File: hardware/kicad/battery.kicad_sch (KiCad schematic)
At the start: 3 parts, among them Q1 AO3407

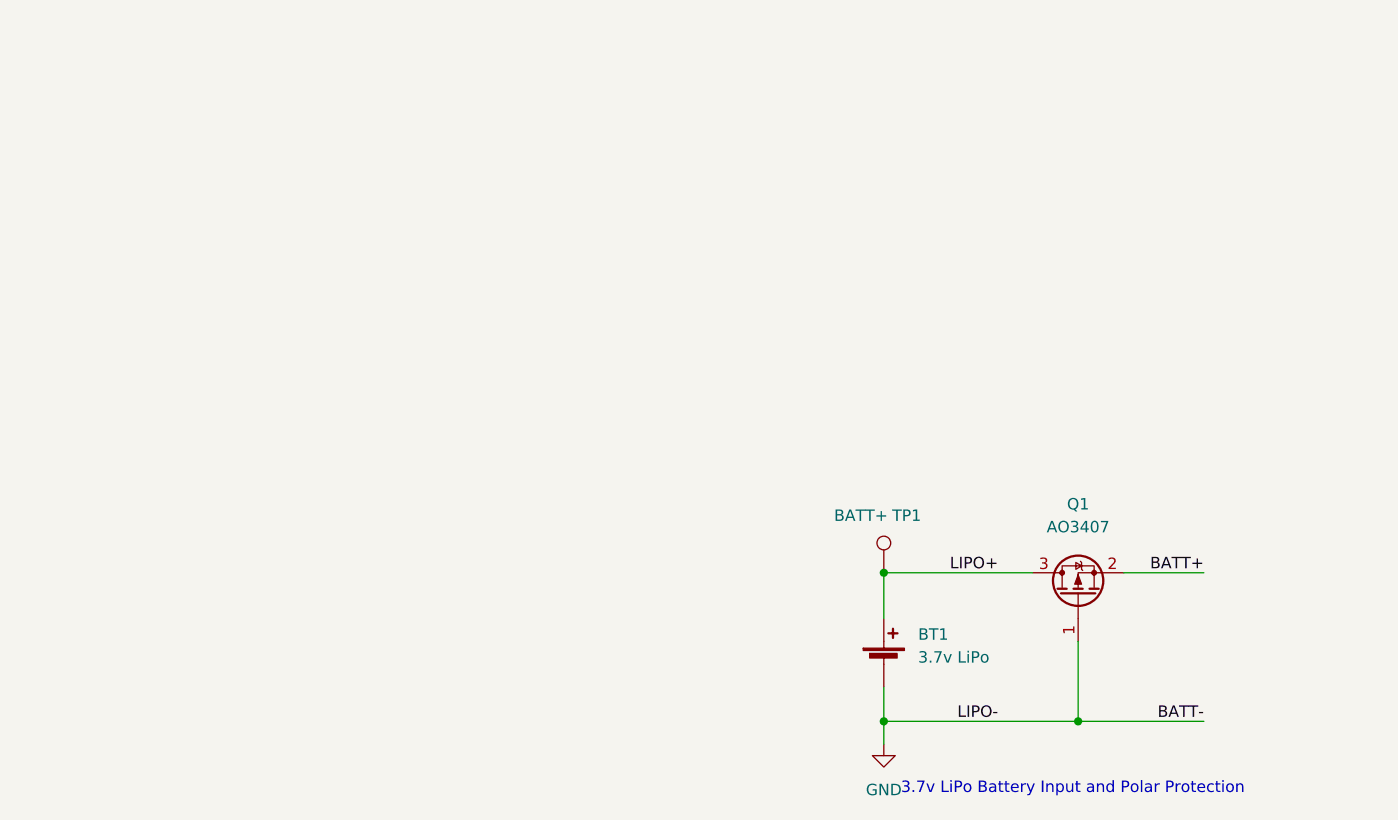
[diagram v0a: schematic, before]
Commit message: fix label
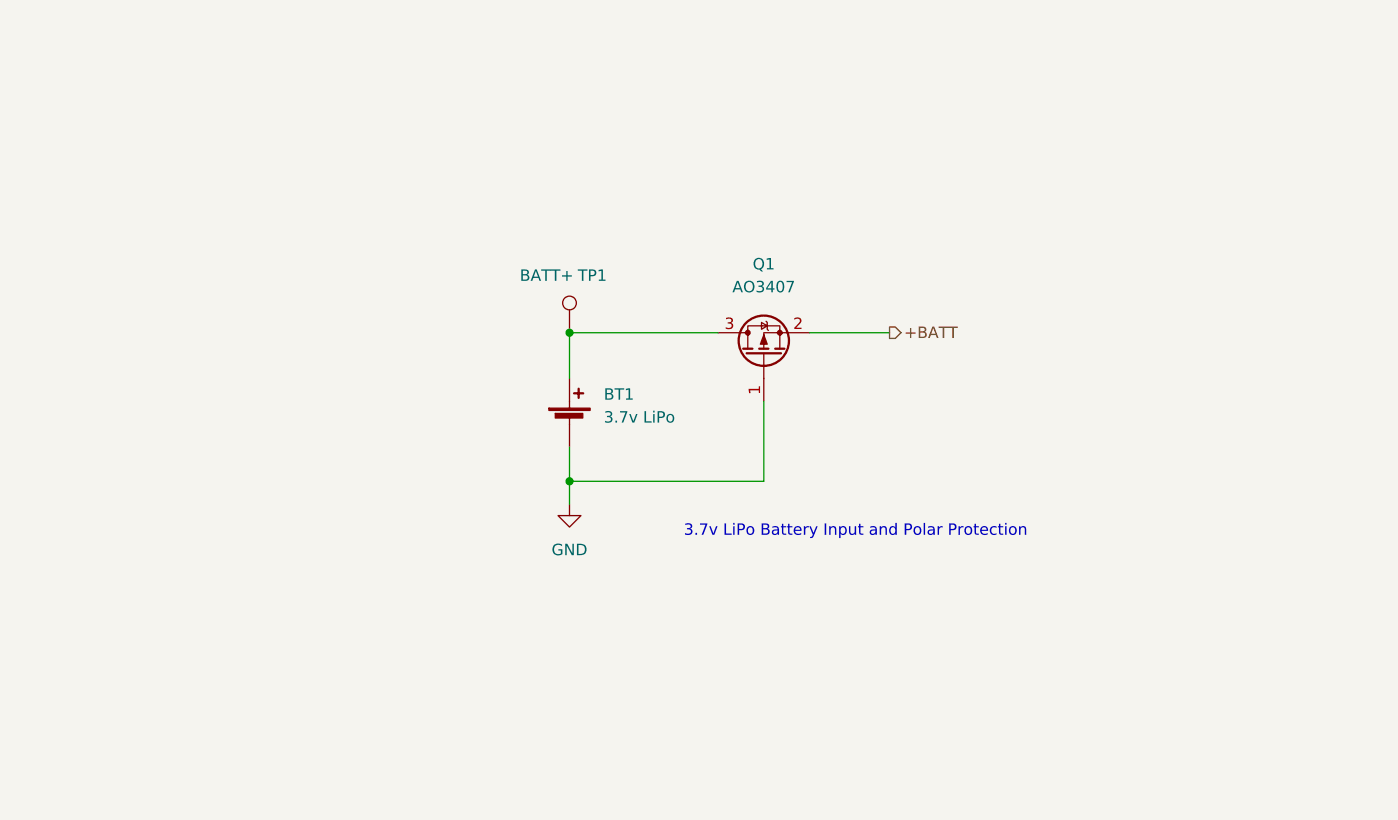
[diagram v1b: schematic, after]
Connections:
- net BATT+ renamed +BATT
- net LIPO+: no longer names the net of BT1.1 (+), Q1.3 (D), TP1.1
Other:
- moved on the sheet: BT1, Q1, TP1
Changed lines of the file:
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@@
 (kicad_sch (version 20230121) (generator eeschema)
-  (paper "A4")
-  (junction (at 114.3 79.375) (diameter 0) (color 0 0 0 0)
+  (paper "A5")
+  (junction (at 79.375 52.705) (diameter 0) (color 0 0 0 0)
   )
-  (junction (at 114.3 95.885) (diameter 0) (color 0 0 0 0)
+  (junction (at 79.375 69.215) (diameter 0) (color 0 0 0 0)
   )
-  (junction (at 135.89 95.885) (diameter 0) (color 0 0 0 0)
-  )
-  (wire (pts (xy 135.89 86.995) (xy 135.89 95.885))
+  (wire (pts (xy 100.965 60.325) (xy 100.965 69.215))
     (stroke (width 0) (type default))
   )
-  (wire (pts (xy 135.89 95.885) (xy 149.86 95.885))
+  (wire (pts (xy 79.375 52.705) (xy 79.375 57.785))
     (stroke (width 0) (type default))
   )
-  (wire (pts (xy 114.3 79.375) (xy 114.3 84.455))
+  (wire (pts (xy 106.045 52.705) (xy 114.935 52.705))
     (stroke (width 0) (type default))
   )
-  (wire (pts (xy 140.97 79.375) (xy 149.86 79.375))
+  (wire (pts (xy 79.375 69.215) (xy 79.375 71.755))
     (stroke (width 0) (type default))
   )
-  (wire (pts (xy 114.3 95.885) (xy 114.3 98.425))
+  (wire (pts (xy 79.375 65.405) (xy 79.375 69.215))
     (stroke (width 0) (type default))
   )
-  (wire (pts (xy 114.3 92.075) (xy 114.3 95.885))
+  (wire (pts (xy 79.375 69.215) (xy 100.965 69.215))
     (stroke (width 0) (type default))
   )
-  (wire (pts (xy 114.3 95.885) (xy 135.89 95.885))
+  (wire (pts (xy 79.375 52.705) (xy 95.885 52.705))
     (stroke (width 0) (type default))
   )
-  (wire (pts (xy 114.3 79.375) (xy 130.81 79.375))
-    (stroke (width 0) (type default))
-  )
-  (text "3.7v LiPo Battery Input and Polar Protection" (at 116.205 104.14 0)
+  (text "3.7v LiPo Battery Input and Polar Protection" (at 92.075 75.565 0)
     (effects (font (size 1.27 1.27)) (justify left bottom))
   )
-  (label "LIPO-" (at 127 95.885 180) (fields_autoplaced)
-    (effects (font (size 1.27 1.27)) (justify right bottom))
+  (hierarchical_label "+BATT" (shape output) (at 114.935 52.705 0) (fields_autoplaced)
+    (effects (font (size 1.27 1.27)) (justify left))
   )
-  (label "LIPO+" (at 127 79.375 180) (fields_autoplaced)
-    (effects (font (size 1.27 1.27)) (justify right bottom))
-  )
-  (label "BATT+" (at 149.86 79.375 180) (fields_autoplaced)
-    (effects (font (size 1.27 1.27)) (justify right bottom))
-  )
-  (label "BATT-" (at 149.86 95.885 180) (fields_autoplaced)
-    (effects (font (size 1.27 1.27)) (justify right bottom))
-  )
-  (symbol (lib_id "Device:Q_PMOS_GSD") (at 135.89 81.915 90) (unit 1)
+  (symbol (lib_id "Device:Q_PMOS_GSD") (at 100.965 55.245 90) (unit 1)
     (in_bom yes) (on_board yes) (dnp no) (fields_autoplaced)
-    (property "Reference" "Q1" (at 135.89 71.755 90)
+    (property "Reference" "Q1" (at 100.965 45.085 90)
       (effects (font (size 1.27 1.27)))
     )
-    (property "Value" "AO3407" (at 135.89 74.295 90)
+    (property "Value" "AO3407" (at 100.965 47.625 90)
       (effects (font (size 1.27 1.27)))
     )
-    (property "Footprint" "Package_TO_SOT_SMD:SOT-23" (at 133.35 76.835 0)
+    (property "Footprint" "Package_TO_SOT_SMD:SOT-23" (at 98.425 50.165 0)
       (effects (font (size 1.27 1.27)) hide)
     )
-    (property "Datasheet" "~" (at 135.89 81.915 0)
+    (property "Datasheet" "~" (at 100.965 55.245 0)
       (effects (font (size 1.27 1.27)) hide)
     )
@@
     )
   )
-  (symbol (lib_id "Connector:TestPoint") (at 114.3 79.375 0) (unit 1)
+  (symbol (lib_id "Connector:TestPoint") (at 79.375 52.705 0) (unit 1)
     (in_bom yes) (on_board yes) (dnp no)
-    (property "Reference" "TP1" (at 116.84 73.025 0)
+    (property "Reference" "TP1" (at 81.915 46.355 0)
       (effects (font (size 1.27 1.27)))
     )
-    (property "Value" "BATT+" (at 111.76 73.025 0)
+    (property "Value" "BATT+" (at 76.835 46.355 0)
       (effects (font (size 1.27 1.27)))
     )
-    (property "Footprint" "TestPoint:TestPoint_Pad_D1.5mm" (at 119.38 79.375 0)
+    (property "Footprint" "TestPoint:TestPoint_Pad_D1.5mm" (at 84.455 52.705 0)
       (effects (font (size 1.27 1.27)) hide)
     )
-    (property "Datasheet" "~" (at 119.38 79.375 0)
+    (property "Datasheet" "~" (at 84.455 52.705 0)
       (effects (font (size 1.27 1.27)) hide)
     )
@@
     )
   )
-  (symbol (lib_id "Device:Battery_Cell") (at 114.3 89.535 0) (unit 1)
+  (symbol (lib_id "Device:Battery_Cell") (at 79.375 62.865 0) (unit 1)
     (in_bom yes) (on_board yes) (dnp no) (fields_autoplaced)
-    (property "Reference" "BT1" (at 118.11 86.2329 0)
+    (property "Reference" "BT1" (at 83.185 59.5629 0)
       (effects (font (size 1.27 1.27)) (justify left))
     )
-    (property "Value" "3.7v LiPo" (at 118.11 88.7729 0)
+    (property "Value" "3.7v LiPo" (at 83.185 62.1029 0)
       (effects (font (size 1.27 1.27)) (justify left))
     )
-    (property "Footprint" "Connector_JST:JST_PH_S2B-PH-K_1x02_P2.00mm_Horizontal" (at 114.3 88.011 90)
+    (property "Footprint" "Connector_JST:JST_PH_S2B-PH-K_1x02_P2.00mm_Horizontal" (at 79.375 61.341 90)
       (effects (font (size 1.27 1.27)) hide)
     )
-    (property "Datasheet" "~" (at 114.3 88.011 90)
+    (property "Datasheet" "~" (at 79.375 61.341 90)
       (effects (font (size 1.27 1.27)) hide)
     )
@@
     )
   )
-  (symbol (lib_id "power:GND") (at 114.3 98.425 0) (unit 1)
+  (symbol (lib_id "power:GND") (at 79.375 71.755 0) (unit 1)
     (in_bom yes) (on_board yes) (dnp no)
-    (property "Reference" "#PWR06" (at 114.3 104.775 0)
+    (property "Reference" "#PWR06" (at 79.375 78.105 0)
       (effects (font (size 1.27 1.27)) hide)
     )
-    (property "Value" "GND" (at 114.3 103.505 0)
+    (property "Value" "GND" (at 79.375 76.835 0)
       (effects (font (size 1.27 1.27)))
     )
-    (property "Footprint" "" (at 114.3 98.425 0)
+    (property "Footprint" "" (at 79.375 71.755 0)
       (effects (font (size 1.27 1.27)) hide)
     )
-    (property "Datasheet" "" (at 114.3 98.425 0)
+    (property "Datasheet" "" (at 79.375 71.755 0)
       (effects (font (size 1.27 1.27)) hide)
     )

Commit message: schematic restructure update
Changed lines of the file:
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@@
+    (stroke (width 0) (type default))
+  )
+  (wire (pts (xy 115.57 48.895) (xy 115.57 52.705))
     (stroke (width 0) (type default))
   )
@@
     (stroke (width 0) (type default))
   )
-  (wire (pts (xy 106.045 52.705) (xy 114.935 52.705))
+  (wire (pts (xy 106.045 52.705) (xy 115.57 52.705))
+    (stroke (width 0) (type default))
+  )
+  (wire (pts (xy 21.59 23.495) (xy 21.59 26.035))
     (stroke (width 0) (type default))
   )
@@
   )
   (wire (pts (xy 79.375 69.215) (xy 100.965 69.215))
+    (stroke (width 0) (type default))
+  )
+  (wire (pts (xy 21.59 26.035) (xy 27.305 26.035))
     (stroke (width 0) (type default))
   )
@@
     (effects (font (size 1.27 1.27)) (justify left bottom))
   )
-  (hierarchical_label "+BATT" (shape output) (at 114.935 52.705 0) (fields_autoplaced)
+  (hierarchical_label "+BATT" (shape bidirectional) (at 27.305 26.035 0) (fields_autoplaced)
     (effects (font (size 1.27 1.27)) (justify left))
   )
@@
         )
         (path "/59b4123e-c7be-466b-a5db-658b8f0c1171/76cc1a03-b597-4ef0-85b8-85a2d617e76b"
+          (reference "Q6") (unit 1)
+        )
+      )
+      (project "bwlr1e"
+        (path "/630c8da6-5464-4eef-824d-89618087f4b4"
           (reference "Q1") (unit 1)
         )
       )
-      (project "bwlr1e"
-        (path "/630c8da6-5464-4eef-824d-89618087f4b4"
-          (reference "Q1") (unit 1)
-        )
-      )
     )
   )
@@
         )
         (path "/59b4123e-c7be-466b-a5db-658b8f0c1171/76cc1a03-b597-4ef0-85b8-85a2d617e76b"
-          (reference "TP1") (unit 1)
+          (reference "TP6") (unit 1)
         )
       )
@@
     )
   )
+  (symbol (lib_id "power:+BATT") (at 115.57 48.895 0) (unit 1)
+    (in_bom yes) (on_board yes) (dnp no)
+    (property "Reference" "#PWR070" (at 115.57 52.705 0)
+      (effects (font (size 1.27 1.27)) hide)
+    )
+    (property "Value" "+BATT" (at 115.57 44.45 0)
+      (effects (font (size 1.27 1.27)))
+    )
+    (property "Footprint" "" (at 115.57 48.895 0)
+      (effects (font (size 1.27 1.27)) hide)
+    )
+    (property "Datasheet" "" (at 115.57 48.895 0)
+      (effects (font (size 1.27 1.27)) hide)
+    )
+    (pin "1")
+    (instances
+      (project "plantpal"
+        (path "/59b4123e-c7be-466b-a5db-658b8f0c1171"
+          (reference "#PWR070") (unit 1)
+        )
+        (path "/59b4123e-c7be-466b-a5db-658b8f0c1171/7fda2409-1758-4461-822b-801ba75fe202"
+          (reference "#PWR050") (unit 1)
+        )
+        (path "/59b4123e-c7be-466b-a5db-658b8f0c1171/76cc1a03-b597-4ef0-85b8-85a2d617e76b"
+          (reference "#PWR078") (unit 1)
+        )
+      )
+      (project "bwlr1e-prog"
+        (path "/630c8da6-5464-4eef-824d-89618087f4b4"
+          (reference "#PWR018") (unit 1)
+        )
+      )
+      (project "feather_rak3172"
+        (path "/a1545928-1195-40b9-b3c4-78f837012afb"
+          (reference "#PWR0131") (unit 1)
+        )
+      )
+    )
+  )
   (symbol (lib_id "power:GND") (at 79.375 71.755 0) (unit 1)
     (in_bom yes) (on_board yes) (dnp no)
@@
         )
         (path "/59b4123e-c7be-466b-a5db-658b8f0c1171/76cc1a03-b597-4ef0-85b8-85a2d617e76b"
-          (reference "#PWR06") (unit 1)
+          (reference "#PWR077") (unit 1)
         )
       )
@@
         )
       )
+    )
+  )
+  (symbol (lib_id "power:+BATT") (at 21.59 23.495 0) (unit 1)
+    (in_bom yes) (on_board yes) (dnp no)
+    (property "Reference" "#PWR070" (at 21.59 27.305 0)
+      (effects (font (size 1.27 1.27)) hide)
+    )
+    (property "Value" "+BATT" (at 21.59 19.05 0)
+      (effects (font (size 1.27 1.27)))
+    )
+    (property "Footprint" "" (at 21.59 23.495 0)
+      (effects (font (size 1.27 1.27)) hide)
+    )
+    (property "Datasheet" "" (at 21.59 23.495 0)
+      (effects (font (size 1.27 1.27)) hide)
+    )
+    (pin "1")
+    (instances
+      (project "plantpal"
+        (path "/59b4123e-c7be-466b-a5db-658b8f0c1171"
+          (reference "#PWR070") (unit 1)
+        )
+        (path "/59b4123e-c7be-466b-a5db-658b8f0c1171/7fda2409-1758-4461-822b-801ba75fe202"
+          (reference "#PWR050") (unit 1)
+        )
+        (path "/59b4123e-c7be-466b-a5db-658b8f0c1171/76cc1a03-b597-4ef0-85b8-85a2d617e76b"
+          (reference "#PWR079") (unit 1)
+        )
+      )
+      (project "bwlr1e-prog"
+        (path "/630c8da6-5464-4eef-824d-89618087f4b4"
+          (reference "#PWR018") (unit 1)
+        )
+      )
+      (project "feather_rak3172"
+        (path "/a1545928-1195-40b9-b3c4-78f837012afb"
+          (reference "#PWR0131") (unit 1)
+        )
+      )

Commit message: beautify schematic
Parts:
- TP1: value BATT+ -> +LIPO
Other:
- note added: "Battery Polar Protection"
- note added: "Sheets Connection"
- note removed: "3.7v LiPo Battery Input and Polar Protection"
- moved on the sheet: BT1, Q1, TP1

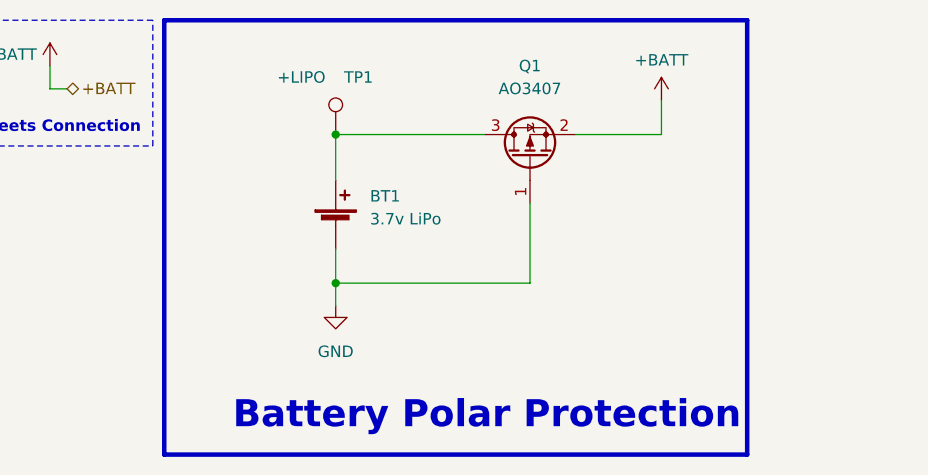
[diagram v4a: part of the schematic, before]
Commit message: battery schematic done
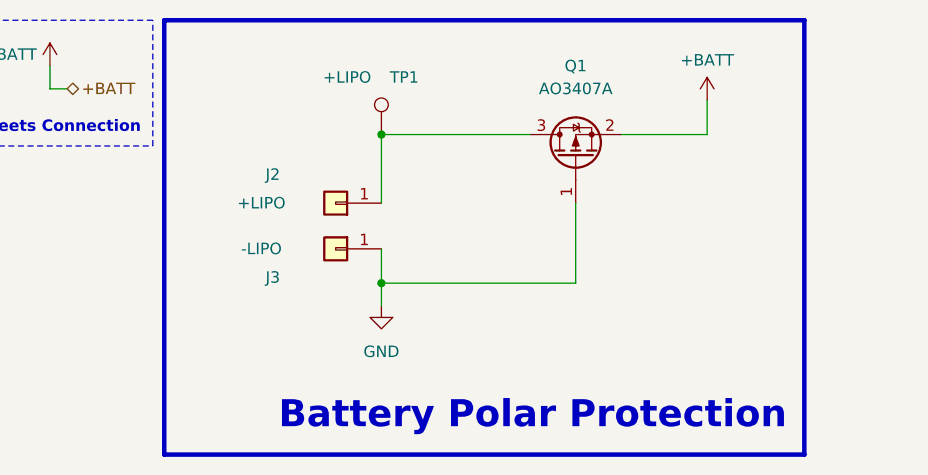
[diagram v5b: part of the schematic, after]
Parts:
- removed BT1: 3.7v LiPo, Connector_JST:JST_PH_S2B-PH-K_1x02_P2.00mm_Horizontal, symbol Device:Battery_Cell
- added J2: +LIPO, TestPoint:TestPoint_Pad_2.0x2.0mm, symbol Connector_Generic:Conn_01x01
- added J3: -LIPO, TestPoint:TestPoint_Pad_2.0x2.0mm, symbol Connector_Generic:Conn_01x01
- Q1: value AO3407 -> AO3407A; Distributor (none) -> LCSC; Distributor Link (none) -> https://www.lcsc.com/product-detail/MOSFETs_Alpha-Omega-Sem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; Distributor Part Number (none) -> C15155; Manufacturer (none) -> Alpha & Omega Semicon; Manufacturer Part Number (none) -> AO3407A; Part Description (none) -> MOSFET P Channel 30V 4.3A 48mΩ@10V,4.3A 1.4W
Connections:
- net GND: now also J3.1 (Pin_1)
- net at Q1.3 (D), TP1.1: now also J2.1 (Pin_1)
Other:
- moved on the sheet: Q1, TP1
